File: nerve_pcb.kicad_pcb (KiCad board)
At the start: 6 copper layers, 50 x 50 mm, 73 parts, among them J1 TC2050-IDC, J2 2171750001, J4 472192001, J5 2x8, J6 2x15, J7 CAN1, J8 CAN2, SW1 SPST, SW2 SPST, U1 ld39150dt33-r, U2 STM32F446RET, U3 BNO085, U4 BMP390, U5 TJA1051T/3, U6 TJA1051T/3, Y1 8M, Y2 32k768, Y3 32k768

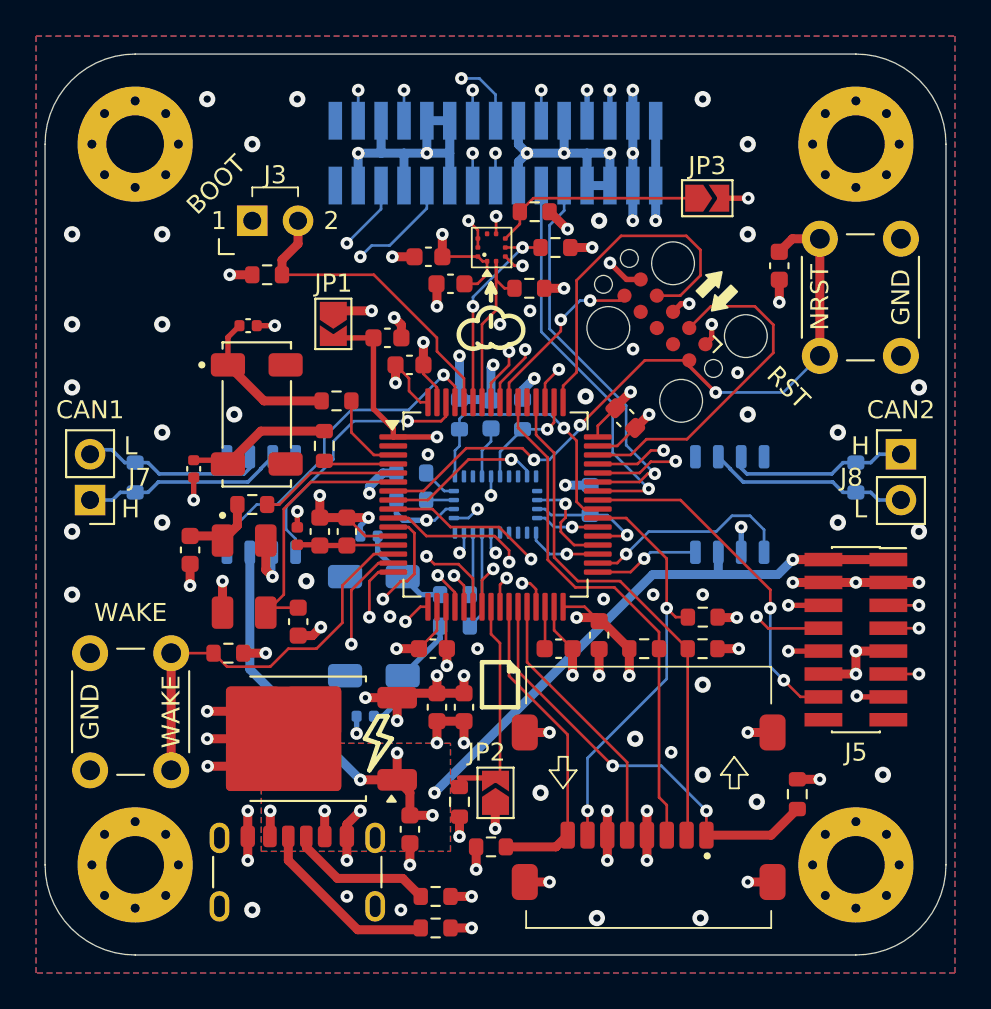
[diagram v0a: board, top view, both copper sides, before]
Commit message: Schematic corrections
- Add decoupling caps for sensor ICs
- Fix clock circuits
- Add BNO085 clock jumper
- Minor cleanup
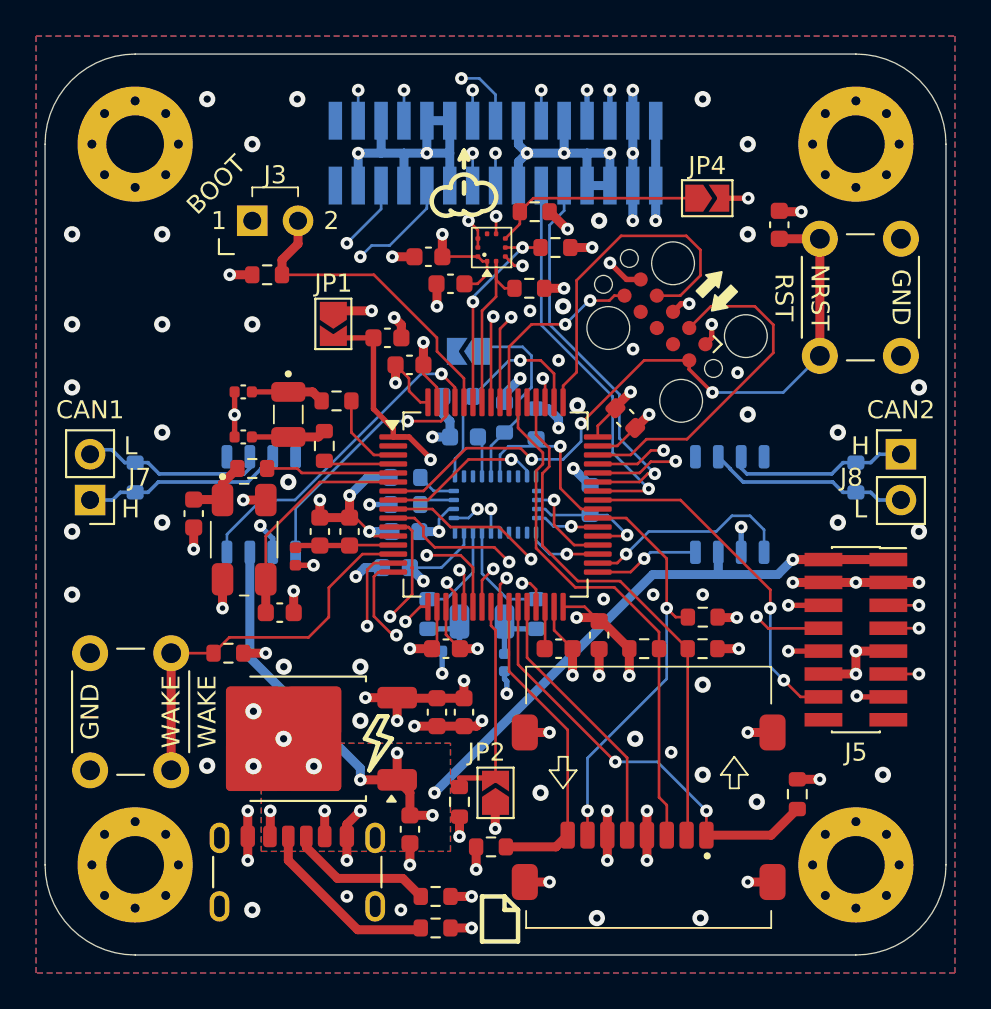
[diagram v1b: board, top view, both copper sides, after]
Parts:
- added C17: 100n, Capacitor_SMD:C_0603_1608Metric, B.Cu at (143.5, 106.5)
- added C18: 100n, Capacitor_SMD:C_0603_1608Metric, B.Cu at (143.0, 108.5)
- added JP3: Open, Jumper:SolderJumper-2_P1.3mm_Open_TrianglePad1.0x1.5mm, B.Cu at (147.0, 96.5)
- added R17: 10k, Resistor_SMD:R_0603_1608Metric, B.Cu at (149.0, 100.2)
- C12, C13: value 20p -> 26p
- C15, C16, C19, C20: value 1p5 -> 15p
- Y1: footprint common:xtal_abm3b-8.000mhz-10-1-u-t -> common:ecs_ecx-64
- Y2, Y3: footprint common:xtal_abs25-32.768khz-6-t -> common:ecs_ecx-34r
- moved C20 8.28 mm to (149.0, 113.8), turned to -90 degrees
- moved C19 7.84 mm to (146.0, 113.1)
- moved Y3 6.01 mm to (147.8, 111.5), turned to 0 degrees
- moved R20 4.55 mm to (150.8, 111.1), turned to -90 degrees
- moved C15 3.68 mm to (134.5, 98.8), turned to 180 degrees
- moved C16 3.27 mm to (134.5, 101.2), turned to 180 degrees
- moved C11 2.28 mm to (164.2, 89.5), turned to -90 degrees
- moved Y1 2.05 mm to (134.6, 107.0)
- moved C12 2.03 mm to (131.8, 105.5)
- moved R11 2.00 mm to (135.0, 103.0)
- moved C21 1.95 mm to (146.8, 101.2), turned to 180 degrees
- moved R19 1.85 mm to (144.8, 111.1), turned to -90 degrees
- moved Y2 1.75 mm to (137.0, 100.0), turned to -90 degrees
- moved C13 1.14 mm to (136.5, 111.0), turned to 0 degrees
- moved L1 1.14 mm to (137.4, 107.9), turned to 90 degrees
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- renumbered C17 to C22, C18 to C23, JP3 to JP4, R17 to R18, R18 to R19, R19 to R20, R20 to R21, R21 to R22, R22 to R23, R23 to R24, R24 to R25, R25 to R26
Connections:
- U2 pad 40: /GPIO_IMU_P0 -> /GPIO_IMU_RST
- U2 pad 50: /GPIO_IMU_RST -> /GPIO_IMU_P0
- U3 pad 10: GND -> Net-(JP3-A)
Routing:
- net Net-(JP3-A): track 0.00 -> 10.7 mm
- net GND: track 132.8 -> 123.7 mm, vias 102 -> 106
- net Net-(C15-Pad1): track 8.48 -> 4.09 mm
- net Net-(C16-Pad1): track 8.09 -> 4.15 mm
- net +3V3: track 74.8 -> 78.4 mm
- net /GPIO_IMU_RST: track 6.16 -> 9.63 mm
- net /GPIO_IMU_P0: track 15.2 -> 12.1 mm
- net Net-(C20-Pad1): track 6.82 -> 3.71 mm
- net /HSE_OUT: track 14.8 -> 12.6 mm
- net /PC3: track 35.5 -> 33.5 mm
- net Net-(U3-XIN32): track 3.51 -> 5.32 mm
- net Net-(C19-Pad1): track 5.31 -> 3.56 mm
- net /CAN1_TX: track 15.1 -> 13.7 mm
- net /PA7: track 31.2 -> 32.4 mm
- net /GPIO_GPS_RST: track 41.4 -> 40.3 mm
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
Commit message: Major stackup revision
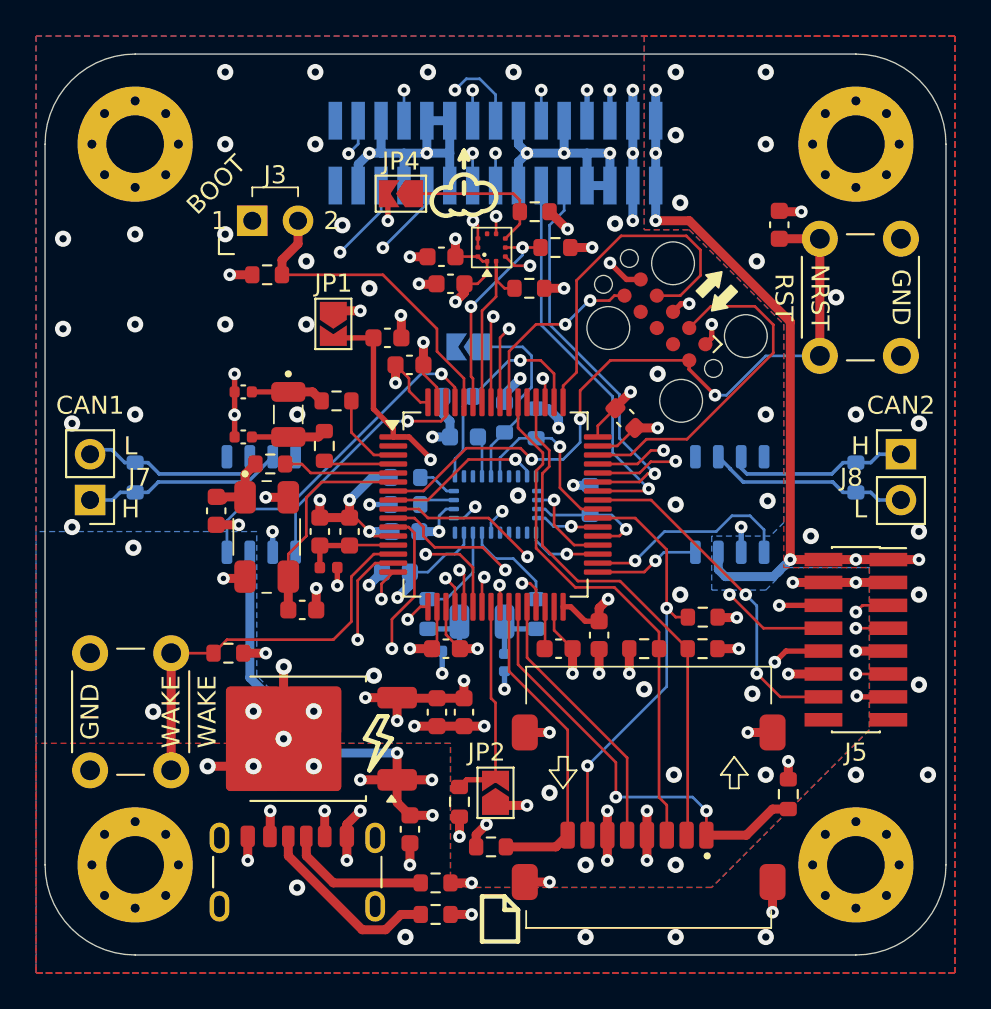
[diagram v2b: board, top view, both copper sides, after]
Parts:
- moved JP4 17.0 mm to (143.2, 87.8), turned to 180 degrees
- moved L1 1.94 mm to (139.2, 108.5), turned to 180 degrees
- moved C12 1.26 mm to (133.0, 105.3)
- moved C13 1.26 mm to (137.8, 110.8)
- moved Y1 1.26 mm to (135.8, 106.8)
- moved R11 1.03 mm to (136.0, 102.8)
- moved R1 0.75 mm to (145.2, 126.0)
- moved R2 0.75 mm to (145.2, 127.8)
- moved C22 0.72 mm to (145.5, 91.2)
- moved R8 0.50 mm to (164.8, 121.1)
- moved JP3 0.25 mm to (147.0, 96.2)
- moved C18 0.25 mm to (143.0, 108.8)
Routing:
- net +5V: track 84.9 -> 94.5 mm, vias 8 -> 12
- net /USART3_RX: track 40.0 -> 34.7 mm
- net /USART2_TX: track 35.9 -> 31.5 mm
- net /USART3_TX: track 46.6 -> 42.4 mm
- net +3V3: track 78.4 -> 74.8 mm, vias 36 -> 35
- net /USART2_RX: track 32.5 -> 29.0 mm
- net +3.3VBATT: track 43.1 -> 46.6 mm
- net Net-(JP4-A): track 11.8 -> 8.49 mm
- net /GPIO_GPS_RST: track 40.3 -> 37.4 mm
- net GND: track 123.7 -> 126.5 mm, vias 106 -> 119
- net /PA7: track 32.4 -> 30.2 mm
- net /PA6: track 29.2 -> 27.6 mm
- net /PA5: track 31.1 -> 32.6 mm
- net /NRST: track 38.4 -> 39.6 mm
- net /HSE_IN: track 7.10 -> 6.21 mm
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- added copper zone on F.Cu, net +3V3
- added copper zone on In2.Cu, net +3V3
- added copper zone on In2.Cu, net +5V
- added copper zone on In3.Cu, net GND
- removed copper zone on In3.Cu, net +3V3
- removed copper zone on In3.Cu, net +5V
- removed copper zone on F.Cu, net GND
- removed copper zone on In2.Cu, net GND

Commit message: Major stackup revision and cleanup
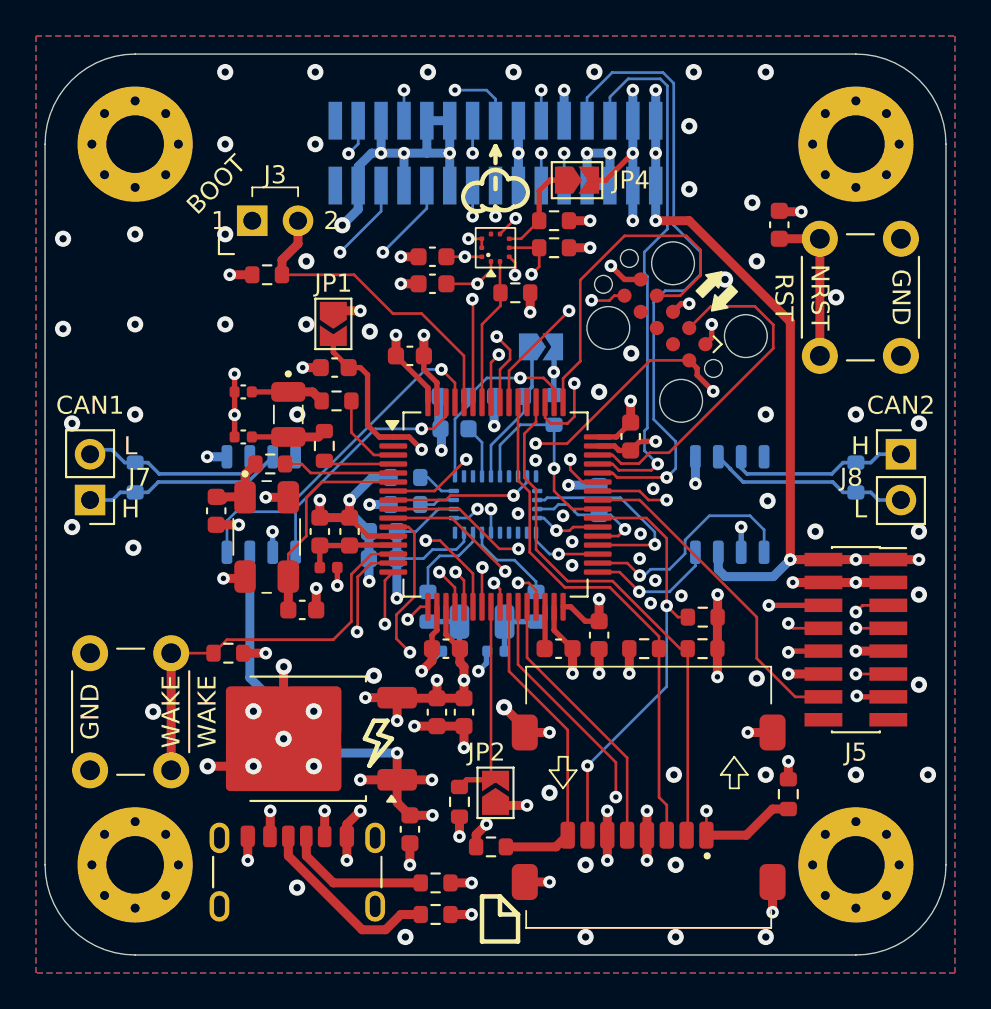
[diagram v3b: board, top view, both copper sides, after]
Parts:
- moved JP4 9.80 mm to (153.0, 87.0), turned to 0 degrees
- moved JP3 4.03 mm to (151.0, 96.2), turned to 0 degrees
- moved C10 3.36 mm to (139.6, 97.4), turned to 180 degrees
- moved C17 1.25 mm to (142.2, 106.5)
- moved R15 1.25 mm to (151.8, 99.8)
- moved R17 1.20 mm to (149.2, 99.0), turned to 180 degrees
- moved R24 1.19 mm to (151.8, 89.2)
- moved C7 1.07 mm to (156.0, 101.2), turned to -90 degrees
- moved C18 1.04 mm to (142.2, 108.0)
- moved C23 1.00 mm to (145.0, 92.8)
- moved R23 0.81 mm to (149.6, 93.2)
- moved C20 0.79 mm to (148.5, 113.1), turned to 180 degrees
- moved C21 0.69 mm to (146.2, 100.8)
- moved C8 0.50 mm to (143.8, 96.8)
- moved C22 0.50 mm to (145.0, 91.2)
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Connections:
- J6 pad 10: /USART1_RX -> /USART1_TX
- J6 pad 12: /USART1_TX -> /USART1_RX
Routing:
- net +5V: track 94.5 -> 71.5 mm
- net +3V3: track 74.8 -> 86.6 mm
- net /SPI2_MOSI: track 5.21 -> 11.2 mm
- net /USART1_CTS: track 29.9 -> 35.7 mm, vias 2 -> 1
- net /USART1_TX: track 22.2 -> 28.0 mm, vias 1 -> 2
- net /GPIO_RADIO_RST: track 19.1 -> 23.9 mm
- net /USART1_RTS: track 26.9 -> 30.7 mm, vias 2 -> 1
- net Net-(JP4-A): track 8.49 -> 5.36 mm
- net /PB5: track 16.8 -> 13.8 mm
- net GND: track 126.5 -> 129.4 mm, vias 119 -> 129
- net /NRST: track 39.6 -> 37.2 mm
- net Net-(JP3-A): track 10.6 -> 8.22 mm
- net /PB4: track 16.7 -> 14.3 mm
- net /I2C1_SCL: track 10.3 -> 8.25 mm
- net /GPIO_IMU_RST: track 9.87 -> 11.7 mm
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- added copper zone on In3.Cu, net +3V3
- added copper zone on In3.Cu, net +5V
- added copper zone on B.Cu, net GND
- added copper zone on F.Cu, net GND
- added copper zone on In2.Cu, net GND
- removed copper zone on B.Cu, net +3V3
- removed copper zone on F.Cu, net +3V3
- removed copper zone on In2.Cu, net +3V3
- removed copper zone on B.Cu, net +5V
- removed copper zone on F.Cu, net +5V
- removed copper zone on In2.Cu, net +5V
- removed copper zone on In3.Cu, net GND

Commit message: Fix HSE clock caps
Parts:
- C12, C13: value 26p -> 30p
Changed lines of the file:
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@@
 			)
 		)
-		(property "Value" "26p"
+		(property "Value" "30p"
 			(at 0 1.43 0)
 			(layer "F.Fab")
@@
 			)
 		)
-		(property "Value" "26p"
+		(property "Value" "30p"
 			(at 0 1.43 -90)
 			(layer "F.Fab")
@@
 		)
 		(property "Value" "Open"
-			(at 0 -1.9 360)
+			(at 0 -1.9 0)
 			(layer "B.Fab")
 			(effects

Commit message: Simplify clock circuits
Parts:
- removed the R11 at (136.0, 102.8)
- removed the R12 at (139.7, 99.2)
- removed the R13 at (139.0, 101.8)
- C12, C13: footprint Capacitor_SMD:C_0603_1608Metric -> Capacitor_SMD:C_0402_1005Metric
- moved C12 3.51 mm to (134.6, 102.2), turned to 90 degrees
- moved C15 2.71 mm to (137.0, 99.8)
- moved C16 2.71 mm to (137.0, 102.2)
- moved Y2 2.46 mm to (139.2, 101.0)
- moved C13 0.31 mm to (137.5, 110.8)
- renumbered R14 to R11, R15 to R12, R16 to R13, R17 to R14, R18 to R15, R19 to R16, R20 to R17, R21 to R18, R22 to R19, R23 to R20, R24 to R21, R25 to R22, R26 to R23
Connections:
- C12 pad 1: Net-(C12-Pad1) -> /HSE_IN
- C15 pad 1: Net-(C15-Pad1) -> /LSE_IN
- C16 pad 1: Net-(C16-Pad1) -> /LSE_OUT
- Y1 pad 1: Net-(C12-Pad1) -> /HSE_IN
- Y2 pad 1: Net-(C15-Pad1) -> /LSE_IN
- Y2 pad 2: Net-(C16-Pad1) -> /LSE_OUT
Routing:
- net /HSE_IN: track 6.21 -> 10.7 mm
- net Net-(C16-Pad1): track 4.15 -> 0.00 mm
- net Net-(C15-Pad1): track 4.09 -> 0.00 mm
- net Net-(C12-Pad1): track 3.70 -> 0.00 mm
- net /LSE_OUT: track 3.90 -> 6.46 mm
- net /LSE_IN: track 4.59 -> 6.80 mm
- net Net-(U2-PA0): track 22.6 -> 21.8 mm
- net +5V: track 71.5 -> 72.3 mm
- net GND: track 129.4 -> 129.7 mm, vias 129 -> 130

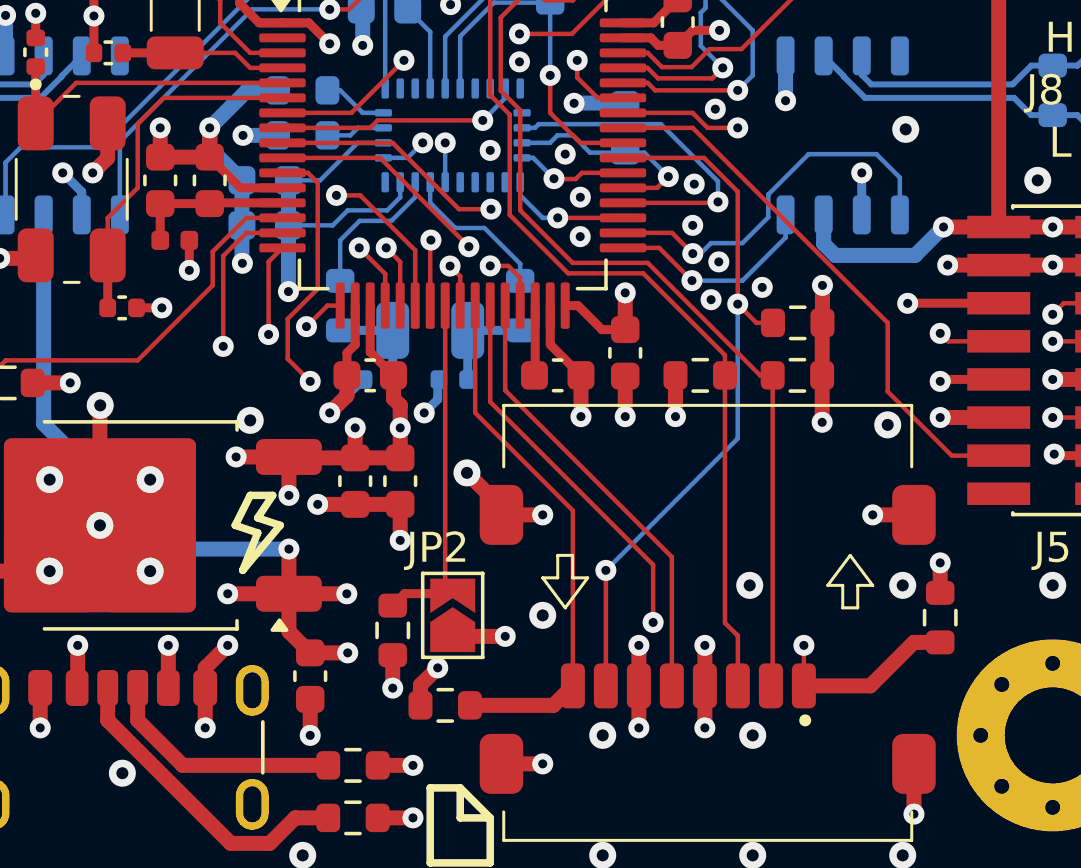
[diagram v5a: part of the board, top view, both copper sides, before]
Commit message: Update IMU clock circuit and cleanup
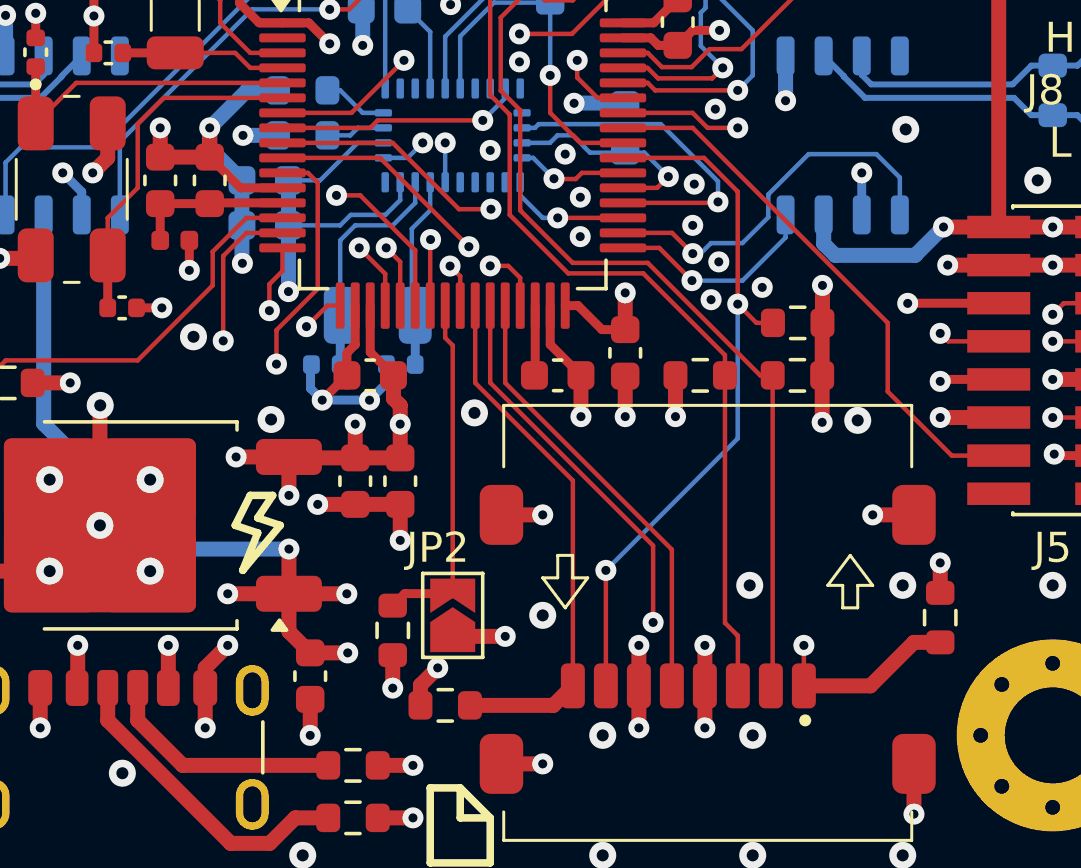
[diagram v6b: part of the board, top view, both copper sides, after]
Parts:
- removed the R16 at (144.8, 110.7)
- removed the R17 at (150.8, 110.7)
- moved C19 1.82 mm to (144.3, 112.6)
- moved C20 1.82 mm to (146.8, 112.6)
- moved Y3 1.82 mm to (146.0, 111.0)
- renumbered R18 to R16, R19 to R17, R20 to R18, R21 to R19, R22 to R20, R23 to R21
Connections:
- C19 pad 1: Net-(C19-Pad1) -> Net-(U3-XIN32)
- C20 pad 1: Net-(C20-Pad1) -> Net-(U3-XOUT32/CLKSEL1)
- Y3 pad 1: Net-(C19-Pad1) -> Net-(U3-XIN32)
- Y3 pad 2: Net-(C20-Pad1) -> Net-(U3-XOUT32/CLKSEL1)
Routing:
- net Net-(C20-Pad1): track 3.39 -> 0.00 mm
- net Net-(C19-Pad1): track 3.39 -> 0.00 mm
- net Net-(U3-XIN32): track 4.94 -> 7.85 mm
- net Net-(U3-XOUT32/CLKSEL1): track 5.10 -> 6.38 mm
- net /PC3: track 31.6 -> 32.3 mm
- net GND: track 129.7 -> 129.3 mm, vias 130 -> 131

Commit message: Swap 32k768 crystal caps to 18pF
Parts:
- C15, C16, C19, C20: value 15p -> 18p
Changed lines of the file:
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@@
 			)
 		)
-		(property "Value" "15p"
+		(property "Value" "18p"
 			(at 0 1.16 0)
 			(layer "F.Fab")
@@
 			)
 		)
-		(property "Value" "15p"
+		(property "Value" "18p"
 			(at -2.02 -0.075 0)
 			(layer "F.Fab")
@@
 			)
 		)
-		(property "Value" "15p"
+		(property "Value" "18p"
 			(at 2.23 0 0)
 			(layer "B.Fab")
@@
 			)
 		)
-		(property "Value" "15p"
+		(property "Value" "18p"
 			(at 2.27 0 0)
 			(layer "B.Fab")
